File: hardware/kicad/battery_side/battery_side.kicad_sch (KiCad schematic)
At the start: 41 parts, among them J1 Conn_01x02, J2 RJ45, J3 USB-OTG, J5 UART-DBG, Q1 AO3401A, Q2 AO3400A, U1 TPS62933FDRLR, U2 R-78E12-1.0, U3 SN65HVD3082E

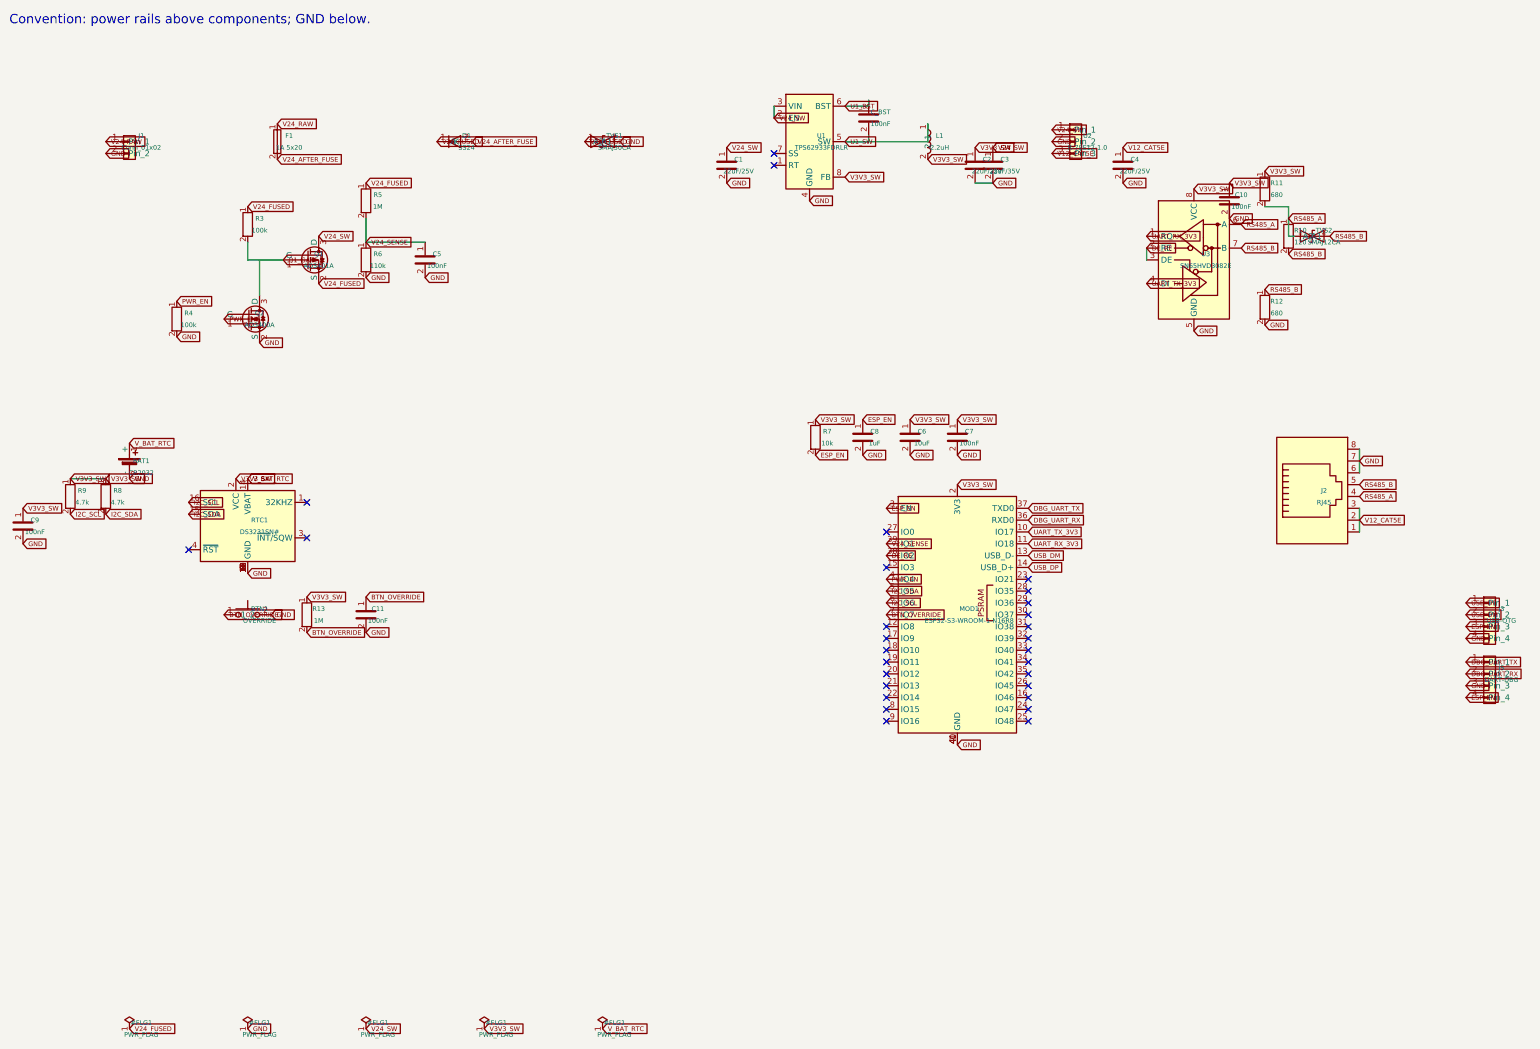
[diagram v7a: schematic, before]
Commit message: hardware: CP-schematic-cleanup iter 40 — Fix A (hide connector pin names)
Codex iter 39 APPROVED iter-37 visual inspection. Iter 40
executes Fix A from §38 fix plan.

Change: added `hide` to the (pin_names ...) clause of every
connector symbol in volthium.kicad_sym:
  - 8P8C        (battery J2, display J1 RJ45s)
  - Conn_01x02  (battery J1 power input)
  - Conn_01x03  (battery U2 R-78E12, display U1 R-78E3.3)
  - Conn_01x04  (battery J3 USB-OTG, J5 UART-DBG;
                 display J3 UART-DBG, J4 USB-OTG)
  - Conn_01x24  (display J2 EPD FFC — the canonical example)

Schematics + PDFs regenerated by build_schematics.py. Pin_N
text removed from every standard connector across both boards.

Visual evidence at visual_inspections/.../iter40/ + before/after
in cp_schematic_cleanup.md §41. Fix A removed one of 2-3
overlapping text layers from every connector region.

Remaining defects (for fixes B-E in future iterations):
  - net-label-vs-pin-number   (fix B: stubs)
  - value-text-vs-symbol-body (fix C: move out)
  - annotation-vs-grid        (fix D: reposition)
  - PWR_FLAG-vs-J1-body       (fix E: reposition)

Audit gates:
  - sch ERC both: 0/0
  - pcb DRC battery_side: 0/0
  - netlist diff vs HEAD: metadata-only (UUID + date)

ITERATION CAP WARNING in §41 + SEMAPHORE note: iter == max (40).
After codex iter-41 review, next claude wake (iter 42) hits
"stuck → user_turn". User decision needed: bump
max_iterations_per_cp or scope B-E into follow-up CP.

SEMAPHORE -> codex_turn iter 41.

Co-Authored-By: Claude Opus 4.7 (1M context) <noreply@anthropic.com>
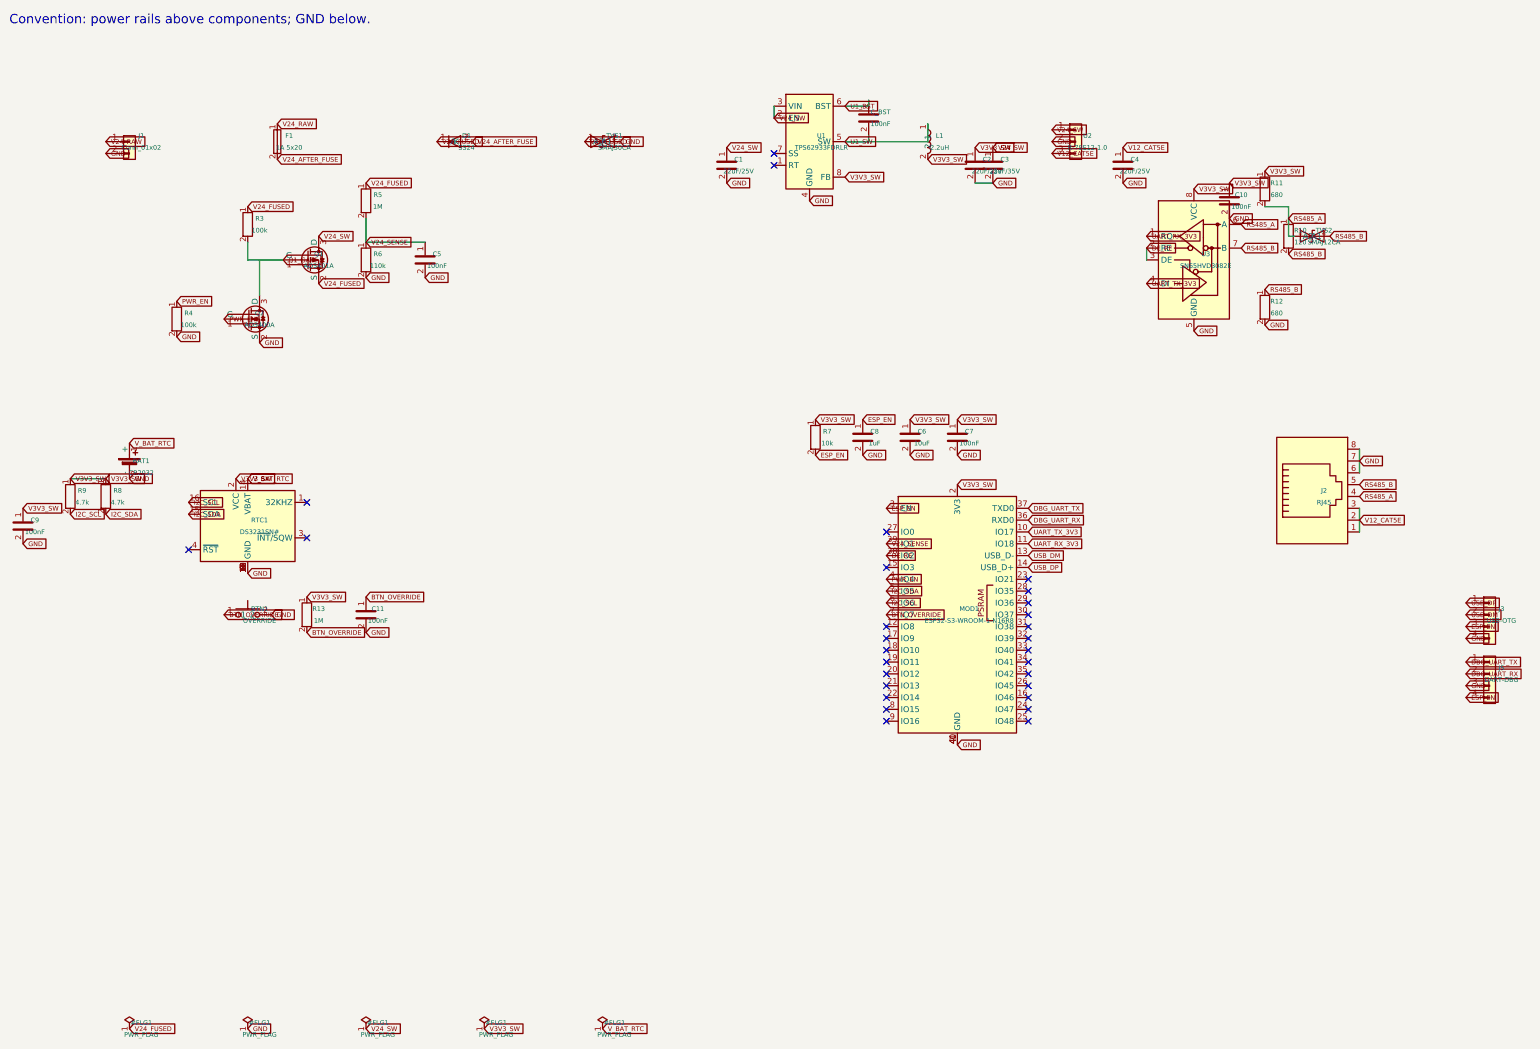
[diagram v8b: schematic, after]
